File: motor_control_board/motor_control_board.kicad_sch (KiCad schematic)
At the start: 30 parts, among them J1 Conn_01x05_Female, J2 Conn_01x05_Female, J3 Harwin_G125-MG10605M4P, J4 Harwin_M80-5000000M5-02-333-0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, J5 Harwin_M80-5400642, J6 Harwin_M80-8510442, J7 Harwin_M80-8510442, U1 CPC1117N

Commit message: components placed
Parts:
- removed TP1: GND, TestPoint:TestPoint_Keystone_5000-5004_Miniature, symbol canhw:TestPoint
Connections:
- net Batt+: now reaches F1.2, J4.1 (Pin_1)
- net ENC2_IN: now reaches J7.2 (Pin_2), R4.1
- net ENC1_IN: now reaches J6.2 (Pin_2), R1.1
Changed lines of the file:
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@@
 	(wire
 		(pts
-			(xy 84.455 187.325) (xy 84.455 190.5)
-		)
-		(stroke
-			(width 0)
-			(type default)
-		)
-	)
-	(wire
-		(pts
 			(xy 83.185 46.355) (xy 114.3 46.355)
 		)
@@
 	(wire
 		(pts
-			(xy 81.28 187.325) (xy 84.455 187.325)
-		)
-		(stroke
-			(width 0)
-			(type default)
-		)
-	)
-	(wire
-		(pts
 			(xy 144.78 105.41) (xy 144.78 96.52)
 		)
@@
 		)
 	)
+	(label "Batt+"
+		(at 88.265 98.425 0)
+		(fields_autoplaced yes)
+		(effects
+			(font
+				(size 1.27 1.27)
+			)
+			(justify left bottom)
+		)
+	)
 	(label "ENC1"
 		(at 107.95 31.115 0)
@@
 		)
 	)
+	(label "ENC1_IN"
+		(at 161.29 141.605 0)
+		(fields_autoplaced yes)
+		(effects
+			(font
+				(size 1.27 1.27)
+			)
+			(justify left bottom)
+		)
+	)
 	(label "CANH"
 		(at 90.17 28.575 180)
@@
 		)
 	)
+	(label "ENC2_IN"
+		(at 228.6 140.97 0)
+		(fields_autoplaced yes)
+		(effects
+			(font
+				(size 1.27 1.27)
+			)
+			(justify left bottom)
+		)
+	)
 	(label "PWM_FS"
 		(at 174.625 105.41 180)
@@
 		(on_board yes)
 		(dnp no)
-		(fields_autoplaced yes)
 		(property "Reference" "J4"
 			(at 83.82 93.98 0)
@@
 		)
 		(property "Value" "Harwin_M80-5000000M5-02-333-00-000"
-			(at 83.82 96.52 0)
+			(at 94.615 77.47 0)
 			(effects
 				(font
@@
 	)
 	(symbol
-		(lib_id "canhw:GND")
-		(at 84.455 190.5 0)
-		(unit 1)
-		(exclude_from_sim no)
-		(in_bom yes)
-		(on_board yes)
-		(dnp no)
-		(fields_autoplaced yes)
-		(property "Reference" "#PWR042"
-			(at 84.455 196.85 0)
-			(effects
-				(font
-					(size 1.27 1.27)
-				)
-				(hide yes)
-			)
-		)
-		(property "Value" "GND"
-			(at 84.455 195.58 0)
-			(effects
-				(font
-					(size 1.27 1.27)
-				)
-				(hide yes)
-			)
-		)
-		(property "Footprint" ""
-			(at 84.455 190.5 0)
-			(effects
-				(font
-					(size 1.27 1.27)
-				)
-				(hide yes)
-			)
-		)
-		(property "Datasheet" ""
-			(at 84.455 190.5 0)
-			(effects
-				(font
-					(size 1.27 1.27)
-				)
-				(hide yes)
-			)
-		)
-		(property "Description" "Power symbol creates a global label with name \"GND\" , ground"
-			(at 84.455 190.5 0)
-			(effects
-				(font
-					(size 1.27 1.27)
-				)
-				(hide yes)
-			)
-		)
-		(property "Purpose" ""
-			(at 84.455 190.5 0)
-			(effects
-				(font
-					(size 1.27 1.27)
-				)
-			)
-		)
-		(pin "1"
-		)
-		(instances
-			(project "Motor Control Board"
-				(path "/ced26b11-410b-4897-bfe1-68b095b3fef4"
-					(reference "#PWR042")
-					(unit 1)
-				)
-			)
-		)
-	)
-	(symbol
 		(lib_id "canhw:D")
 		(at 99.695 142.24 180)
@@
 					(unit 1)
 				)
-			)
-		)
-	)
-	(symbol
-		(lib_id "canhw:TestPoint")
-		(at 81.28 187.325 90)
-		(unit 1)
-		(exclude_from_sim no)
-		(in_bom yes)
-		(on_board yes)
-		(dnp no)
-		(fields_autoplaced yes)
-		(property "Reference" "TP1"
-			(at 77.978 182.245 90)
-			(effects
-				(font
-					(size 1.27 1.27)
-				)
-			)
-		)
-		(property "Value" "GND"
-			(at 77.978 184.785 90)
-			(effects
-				(font
-					(size 1.27 1.27)
-				)
-			)
-		)
-		(property "Footprint" "TestPoint:TestPoint_Keystone_5000-5004_Miniature"
-			(at 81.28 182.245 0)
-			(effects
-				(font
-					(size 1.27 1.27)
-				)
-				(hide yes)
-			)
-		)
-		(property "Datasheet" "~"
-			(at 81.28 182.245 0)
-			(effects
-				(font
-					(size 1.27 1.27)
-				)
-				(hide yes)
-			)
-		)
-		(property "Description" "test point"
-			(at 81.28 187.325 0)
-			(effects
-				(font
-					(size 1.27 1.27)
-				)
-				(hide yes)
-			)
-		)
-		(pin "1"
-		)
-		(instances
-			(project ""
-				(path "/ced26b11-410b-4897-bfe1-68b095b3fef4"
-					(reference "TP1")
-					(unit 1)
-				)

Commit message: PCB routing 70% done
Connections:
- net +12V: no longer F2.1
- net Batt+: now also F2.1
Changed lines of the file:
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@@
 	(wire
 		(pts
-			(xy 109.855 125.73) (xy 109.855 130.175)
+			(xy 109.855 123.19) (xy 109.855 130.175)
 		)
 		(stroke
@@
 			)
 			(justify right bottom)
+		)
+	)
+	(label "Batt+"
+		(at 109.855 123.19 0)
+		(fields_autoplaced yes)
+		(effects
+			(font
+				(size 1.27 1.27)
+			)
+			(justify left bottom)
 		)
 	)
@@
 					(unit 1)
 				)
-			)
-		)
-	)
-	(symbol
-		(lib_id "canhw:+12V")
-		(at 109.855 125.73 0)
-		(unit 1)
-		(exclude_from_sim no)
-		(in_bom yes)
-		(on_board yes)
-		(dnp no)
-		(fields_autoplaced yes)
-		(property "Reference" "#PWR011"
-			(at 109.855 129.54 0)
-			(effects
-				(font
-					(size 1.27 1.27)
-				)
-				(hide yes)
-			)
-		)
-		(property "Value" "+12V"
-			(at 109.855 120.65 0)
-			(effects
-				(font
-					(size 1.27 1.27)
-				)
-			)
-		)
-		(property "Footprint" ""
-			(at 109.855 125.73 0)
-			(effects
-				(font
-					(size 1.27 1.27)
-				)
-				(hide yes)
-			)
-		)
-		(property "Datasheet" ""
-			(at 109.855 125.73 0)
-			(effects
-				(font
-					(size 1.27 1.27)
-				)
-				(hide yes)
-			)
-		)
-		(property "Description" "Power symbol creates a global label with name \"+12V\""
-			(at 109.855 125.73 0)
-			(effects
-				(font
-					(size 1.27 1.27)
-				)
-				(hide yes)
-			)
-		)
-		(pin "1"
-		)
-		(instances
-			(project "Motor Control Board"
-				(path "/ced26b11-410b-4897-bfe1-68b095b3fef4"
-					(reference "#PWR011")
-					(unit 1)
-				)

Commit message: Fixed symbol and footprint libraries
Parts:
- J6, J7: symbol Connector:Conn_01x04_Pin -> canhw:Conn_01x04_Pin
- R26: symbol Device:R_US -> canhw:R_US
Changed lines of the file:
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@@
 	)
 	(symbol
-		(lib_id "Connector:Conn_01x04_Pin")
+		(lib_id "canhw:Conn_01x04_Pin")
 		(at 223.52 140.97 0)
 		(unit 1)
@@
 	)
 	(symbol
-		(lib_id "Device:R_US")
+		(lib_id "canhw:R_US")
 		(at 229.235 92.71 0)
 		(unit 1)
@@
 	)
 	(symbol
-		(lib_id "Connector:Conn_01x04_Pin")
+		(lib_id "canhw:Conn_01x04_Pin")
 		(at 156.21 141.605 0)
 		(unit 1)

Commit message: Fixed DRC errors except for the PTH keep out zones
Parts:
- J4: footprint motor-control:HARWIN_M80-5000000M5-02-333-00-000 -> canhw_footprints:HARWIN_M80-5000000M5-02-333-00-000
- J5: footprint motor-control:HARWIN_M80-5400642 -> canhw_footprints:HARWIN_M80-5400642
- J6, J7: footprint motor-control:HARWIN_M80-8510442 -> canhw_footprints:HARWIN_M80-8510442
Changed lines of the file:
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@@
 			)
 		)
-		(property "Footprint" "motor-control:HARWIN_M80-8510442"
+		(property "Footprint" "canhw_footprints:HARWIN_M80-8510442"
 			(at 223.52 140.97 0)
 			(effects
@@
 			)
 		)
-		(property "Footprint" "motor-control:HARWIN_M80-5000000M5-02-333-00-000"
+		(property "Footprint" "canhw_footprints:HARWIN_M80-5000000M5-02-333-00-000"
 			(at 83.185 98.425 0)
 			(effects
@@
 			)
 		)
-		(property "Footprint" "motor-control:HARWIN_M80-8510442"
+		(property "Footprint" "canhw_footprints:HARWIN_M80-8510442"
 			(at 156.21 141.605 0)
 			(effects
@@
 			)
 		)
-		(property "Footprint" "motor-control:HARWIN_M80-5400642"
+		(property "Footprint" "canhw_footprints:HARWIN_M80-5400642"
 			(at 128.905 105.41 0)
 			(effects

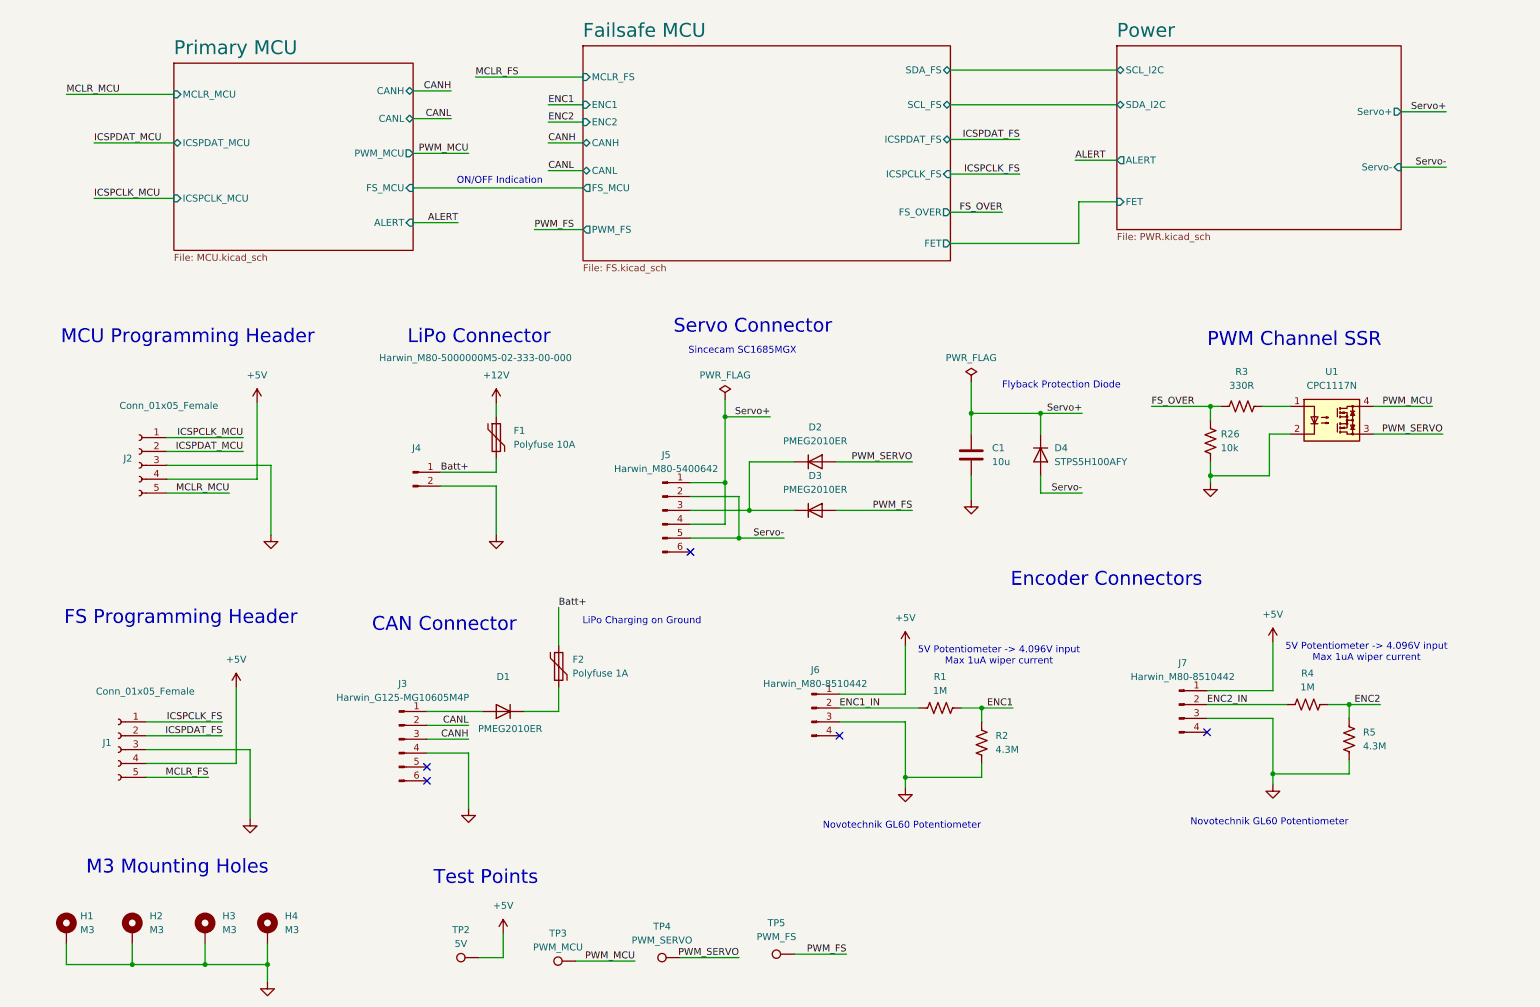
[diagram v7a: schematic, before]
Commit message: Added servo power LED, bulk decoupling caps
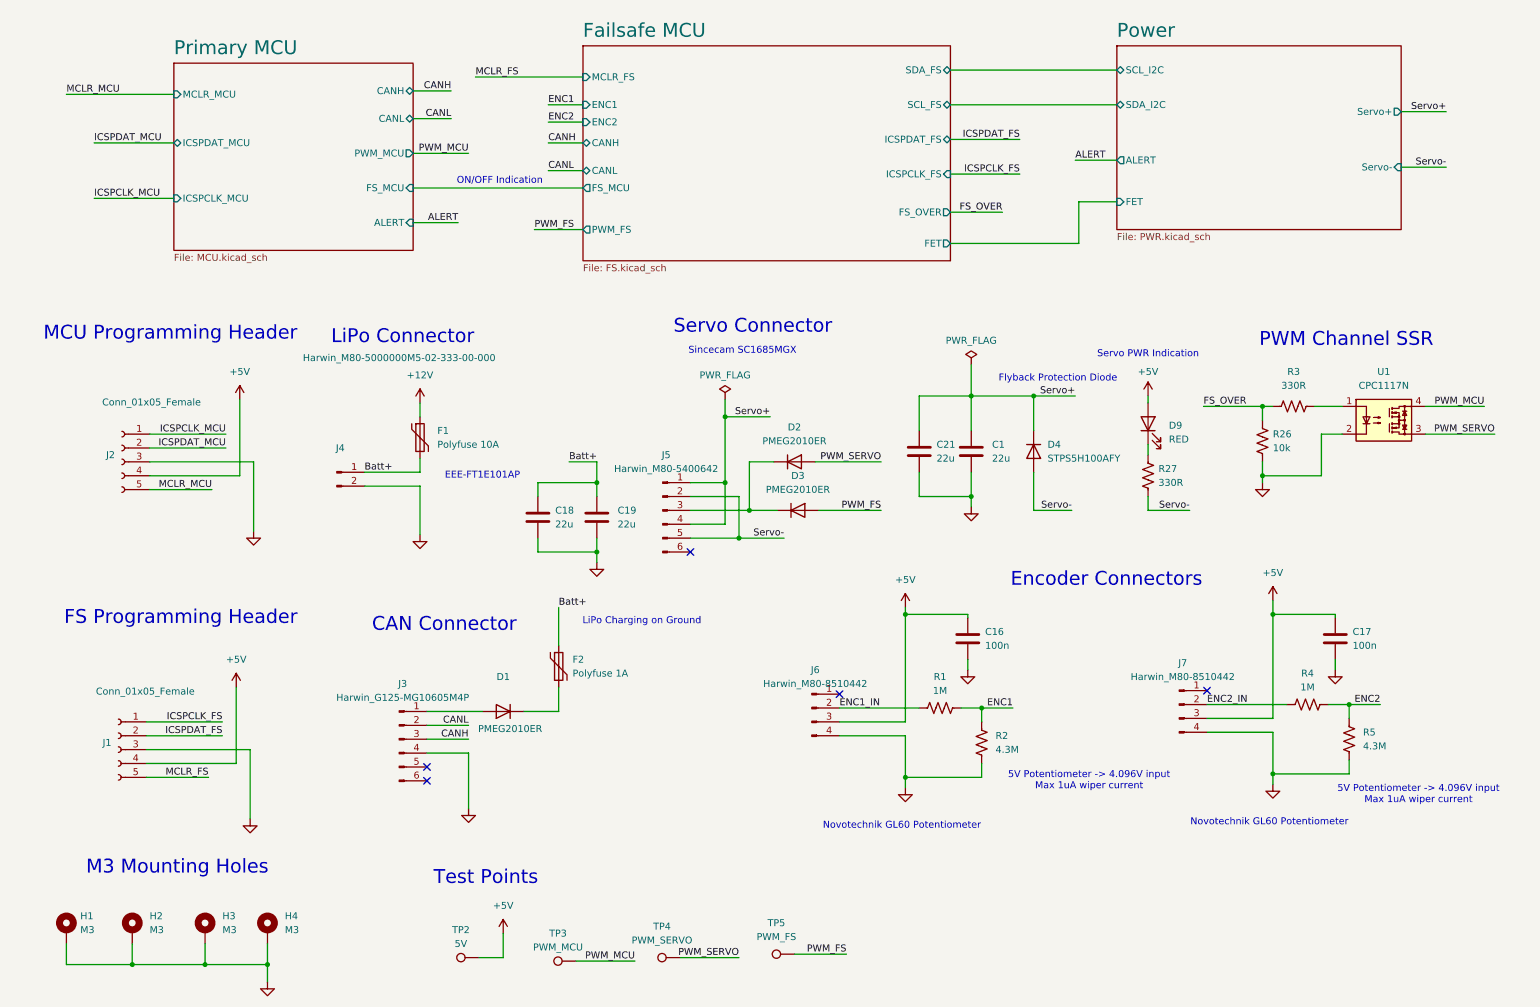
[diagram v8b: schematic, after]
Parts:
- added C16, C17: 100n, Capacitor_SMD:C_0805_2012Metric_Pad1.18x1.45mm_HandSolder, symbol canhw:C
- added C18, C19, C21: 22u, Capacitor_SMD:C_0805_2012Metric_Pad1.18x1.45mm_HandSolder, symbol canhw:C
- added D9: RED, LED_SMD:LED_1206_3216Metric_Pad1.42x1.75mm_HandSolder, symbol canhw:LED
- added R27: 330R, Resistor_SMD:R_0805_2012Metric_Pad1.20x1.40mm_HandSolder, symbol Device:R_US
- C1: value 10u -> 22u
- U1: footprint Package_SO:SOP-4_3.8x4.1mm_P2.54mm -> canhw_footprints:SOIC254P610X218-4N
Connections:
- net +5V: now also J6.3 (Pin_3), J7.3 (Pin_3), C16.1, C17.1, D9.2 (A); no longer J6.1 (Pin_1), J7.1 (Pin_1)
- net Batt+: now also C18.1, C19.1
- net GND: now also J6.4 (Pin_4), J7.4 (Pin_4), C16.2, C17.2, C18.2, C19.2, C21.2; no longer J6.3 (Pin_3), J7.3 (Pin_3)
- net Servo+: now also C21.1
- net Servo-: now also R27.2
- new net: D9.1 (K), R27.1
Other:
- note added: "EEE-FT1E101AP"
- note added: "Servo PWR Indication"
- moved on the sheet: C1, D2, D3, D4, F1, J2, J4, R26, R3, U1
